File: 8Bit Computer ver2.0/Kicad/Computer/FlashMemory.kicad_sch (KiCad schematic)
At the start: 30 parts, among them IC189 SN74AHC74DR, IC190 M29F800FT55N3E2, IC191 DS1100Z-20+, IC192 M29F800FT55N3E2, IC193 SN74ABT245BDWR, IC194 SN74ABT245BDWR, IC195 SN74ABT245BDWR, IC196 SN74ABT245BDWR, IC197 SN74ABT245BDWR, IC198 SN74ABT245BDWR, IC199 SN74ABT245BDWR, IC200 SN74ABT245BDWR, IC201 SN74ABT245BDWR, IC202 SN74ABT245BDWR, IC203 SN74ABT245BDWR, IC204 SN74ABT245BDWR, IC205 SN74ABT245BDWR, IC206 SN74ABT245BDWR, J1 Conn_02x25_Odd_Even, J2 Conn_02x25_Odd_Even

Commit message: Kicad SCH/PCB
Kicad SCH/PCB:
changed the References in SCH
began with INOUTPUT module nearly done
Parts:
- renumbered IC191 to IC198, IC189 to IC199, IC194 to IC200, IC193 to IC201, IC197 to IC202, IC200 to IC203, IC201 to IC204, IC192 to IC205, IC202 to IC206, IC190 to IC207, IC195 to IC208, IC196 to IC209, IC203 to IC210, IC204 to IC211, IC198 to IC212, IC199 to IC213, IC205 to IC214, IC206 to IC215, J1 to J35, J2 to J36, R2 to R21, R1 to R22, R4 to R23, R6 to R24, R7 to R25, R8 to R26, R3 to R27, R5 to R28, R9 to R29, R10 to R30
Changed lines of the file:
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@@
 		(dnp no)
 		(fields_autoplaced yes)
-		(property "Reference" "IC191"
+		(property "Reference" "IC198"
 			(at 163.83 255.27 0)
 			(effects
@@
 			(project ""
 				(path "/1196a00e-6878-4d6d-82b7-9e052dfe7c14/51d10ac8-27e7-4c9f-83ea-98776ebc8169"
-					(reference "IC191")
+					(reference "IC198")
 					(unit 1)
 				)
@@
 		(dnp no)
 		(fields_autoplaced yes)
-		(property "Reference" "R5"
+		(property "Reference" "R28"
 			(at 449.58 397.5099 0)
 			(effects
@@
 			(project "Computer"
 				(path "/1196a00e-6878-4d6d-82b7-9e052dfe7c14/51d10ac8-27e7-4c9f-83ea-98776ebc8169"
-					(reference "R5")
+					(reference "R28")
 					(unit 1)
 				)
@@
 		(dnp no)
 		(fields_autoplaced yes)
-		(property "Reference" "IC204"
+		(property "Reference" "IC211"
 			(at 505.46 236.22 0)
 			(effects
@@
 			(project "Computer"
 				(path "/1196a00e-6878-4d6d-82b7-9e052dfe7c14/51d10ac8-27e7-4c9f-83ea-98776ebc8169"
-					(reference "IC204")
+					(reference "IC211")
 					(unit 1)
 				)
@@
 		(dnp no)
 		(fields_autoplaced yes)
-		(property "Reference" "J1"
+		(property "Reference" "J35"
 			(at 262.89 105.4099 90)
 			(effects
@@
 			(project ""
 				(path "/1196a00e-6878-4d6d-82b7-9e052dfe7c14/51d10ac8-27e7-4c9f-83ea-98776ebc8169"
-					(reference "J1")
+					(reference "J35")
 					(unit 1)
 				)
@@
 		(dnp no)
 		(fields_autoplaced yes)
-		(property "Reference" "IC205"
+		(property "Reference" "IC214"
 			(at 567.69 203.2 0)
 			(effects
@@
 			(project "Computer"
 				(path "/1196a00e-6878-4d6d-82b7-9e052dfe7c14/51d10ac8-27e7-4c9f-83ea-98776ebc8169"
-					(reference "IC205")
+					(reference "IC214")
 					(unit 1)
 				)
@@
 		(dnp no)
 		(fields_autoplaced yes)
-		(property "Reference" "R2"
+		(property "Reference" "R21"
 			(at 252.73 342.8999 0)
 			(effects
@@
 			(project "Computer"
 				(path "/1196a00e-6878-4d6d-82b7-9e052dfe7c14/51d10ac8-27e7-4c9f-83ea-98776ebc8169"
-					(reference "R2")
+					(reference "R21")
 					(unit 1)
 				)
@@
 		(dnp no)
 		(fields_autoplaced yes)
-		(property "Reference" "IC189"
+		(property "Reference" "IC199"
 			(at 219.71 292.1 0)
 			(effects
@@
 			(project ""
 				(path "/1196a00e-6878-4d6d-82b7-9e052dfe7c14/51d10ac8-27e7-4c9f-83ea-98776ebc8169"
-					(reference "IC189")
+					(reference "IC199")
 					(unit 1)
 				)
@@
 		(dnp no)
 		(fields_autoplaced yes)
-		(property "Reference" "IC193"
+		(property "Reference" "IC201"
 			(at 224.79 342.9 0)
 			(effects
@@
 			(project ""
 				(path "/1196a00e-6878-4d6d-82b7-9e052dfe7c14/51d10ac8-27e7-4c9f-83ea-98776ebc8169"
-					(reference "IC193")
+					(reference "IC201")
 					(unit 1)
 				)
@@
 		(dnp no)
 		(fields_autoplaced yes)
-		(property "Reference" "IC194"
+		(property "Reference" "IC200"
 			(at 223.52 386.08 0)
 			(effects
@@
 			(project "Computer"
 				(path "/1196a00e-6878-4d6d-82b7-9e052dfe7c14/51d10ac8-27e7-4c9f-83ea-98776ebc8169"
-					(reference "IC194")
+					(reference "IC200")
 					(unit 1)
 				)
@@
 		(dnp no)
 		(fields_autoplaced yes)
-		(property "Reference" "IC198"
+		(property "Reference" "IC212"
 			(at 513.08 350.52 0)
 			(effects
@@
 			(project "Computer"
 				(path "/1196a00e-6878-4d6d-82b7-9e052dfe7c14/51d10ac8-27e7-4c9f-83ea-98776ebc8169"
-					(reference "IC198")
+					(reference "IC212")
 					(unit 1)
 				)
@@
 		(dnp no)
 		(fields_autoplaced yes)
-		(property "Reference" "R7"
+		(property "Reference" "R25"
 			(at 287.02 227.3299 0)
 			(effects
@@
 			(project "Computer"
 				(path "/1196a00e-6878-4d6d-82b7-9e052dfe7c14/51d10ac8-27e7-4c9f-83ea-98776ebc8169"
-					(reference "R7")
+					(reference "R25")
 					(unit 1)
 				)
@@
 		(dnp no)
 		(fields_autoplaced yes)
-		(property "Reference" "IC196"
+		(property "Reference" "IC209"
 			(at 426.72 397.51 0)
 			(effects
@@
 			(project "Computer"
 				(path "/1196a00e-6878-4d6d-82b7-9e052dfe7c14/51d10ac8-27e7-4c9f-83ea-98776ebc8169"
-					(reference "IC196")
+					(reference "IC209")
 					(unit 1)
 				)
@@
 		(dnp no)
 		(fields_autoplaced yes)
-		(property "Reference" "IC202"
+		(property "Reference" "IC206"
 			(at 355.6 288.29 0)
 			(effects
@@
 			(project "Computer"
 				(path "/1196a00e-6878-4d6d-82b7-9e052dfe7c14/51d10ac8-27e7-4c9f-83ea-98776ebc8169"
-					(reference "IC202")
+					(reference "IC206")
 					(unit 1)
 				)
@@
 		(dnp no)
 		(fields_autoplaced yes)
-		(property "Reference" "R4"
+		(property "Reference" "R23"
 			(at 261.62 443.2299 0)
 			(effects
@@
 			(project "Computer"
 				(path "/1196a00e-6878-4d6d-82b7-9e052dfe7c14/51d10ac8-27e7-4c9f-83ea-98776ebc8169"
-					(reference "R4")
+					(reference "R23")
 					(unit 1)
 				)
@@
 		(dnp no)
 		(fields_autoplaced yes)
-		(property "Reference" "IC192"
+		(property "Reference" "IC205"
 			(at 303.53 347.98 0)
 			(effects
@@
 			(project "Computer"
 				(path "/1196a00e-6878-4d6d-82b7-9e052dfe7c14/51d10ac8-27e7-4c9f-83ea-98776ebc8169"
-					(reference "IC192")
+					(reference "IC205")
 					(unit 1)
 				)
@@
 		(dnp no)
 		(fields_autoplaced yes)
-		(property "Reference" "IC199"
+		(property "Reference" "IC213"
 			(at 513.08 394.97 0)
 			(effects
@@
 			(project "Computer"
 				(path "/1196a00e-6878-4d6d-82b7-9e052dfe7c14/51d10ac8-27e7-4c9f-83ea-98776ebc8169"
-					(reference "IC199")
+					(reference "IC213")
 					(unit 1)
 				)
@@
 		(dnp no)
 		(fields_autoplaced yes)
-		(property "Reference" "J2"
+		(property "Reference" "J36"
 			(at 438.15 105.4099 90)
 			(effects
@@
 			(project "Computer"
 				(path "/1196a00e-6878-4d6d-82b7-9e052dfe7c14/51d10ac8-27e7-4c9f-83ea-98776ebc8169"
-					(reference "J2")
+					(reference "J36")
 					(unit 1)
 				)
@@
 		(dnp no)
 		(fields_autoplaced yes)
-		(property "Reference" "IC206"
+		(property "Reference" "IC215"
 			(at 567.69 238.76 0)
 			(effects
@@
 			(project "Computer"
 				(path "/1196a00e-6878-4d6d-82b7-9e052dfe7c14/51d10ac8-27e7-4c9f-83ea-98776ebc8169"
-					(reference "IC206")
+					(reference "IC215")
 					(unit 1)
 				)
@@
 		(dnp no)
 		(fields_autoplaced yes)
-		(property "Reference" "IC197"
+		(property "Reference" "IC202"
 			(at 233.68 443.23 0)
 			(effects
@@
 			(project "Computer"
 				(path "/1196a00e-6878-4d6d-82b7-9e052dfe7c14/51d10ac8-27e7-4c9f-83ea-98776ebc8169"
-					(reference "IC197")
+					(reference "IC202")
 					(unit 1)
 				)
@@
 		(dnp no)
 		(fields_autoplaced yes)
-		(property "Reference" "IC190"
+		(property "Reference" "IC207"
 			(at 387.35 196.85 0)
 			(effects
@@
 			(project ""
 				(path "/1196a00e-6878-4d6d-82b7-9e052dfe7c14/51d10ac8-27e7-4c9f-83ea-98776ebc8169"
-					(reference "IC190")
+					(reference "IC207")
 					(unit 1)
 				)
@@
 		(dnp no)
 		(fields_autoplaced yes)
-		(property "Reference" "R6"
+		(property "Reference" "R24"
 			(at 287.02 184.1499 0)
 			(effects
@@
 			(project "Computer"
 				(path "/1196a00e-6878-4d6d-82b7-9e052dfe7c14/51d10ac8-27e7-4c9f-83ea-98776ebc8169"
-					(reference "R6")
+					(reference "R24")
 					(unit 1)
 				)
@@
 		(dnp no)
 		(fields_autoplaced yes)
-		(property "Reference" "IC200"
+		(property "Reference" "IC203"
 			(at 259.08 184.15 0)
 			(effects
@@
 			(project "Computer"
 				(path "/1196a00e-6878-4d6d-82b7-9e052dfe7c14/51d10ac8-27e7-4c9f-83ea-98776ebc8169"
-					(reference "IC200")
+					(reference "IC203")
 					(unit 1)
 				)
@@
 		(dnp no)
 		(fields_autoplaced yes)
-		(property "Reference" "IC201"
+		(property "Reference" "IC204"
 			(at 259.08 227.33 0)
 			(effects
@@
 			(project "Computer"
 				(path "/1196a00e-6878-4d6d-82b7-9e052dfe7c14/51d10ac8-27e7-4c9f-83ea-98776ebc8169"
-					(reference "IC201")
+					(reference "IC204")
 					(unit 1)
 				)
@@
 		(dnp no)
 		(fields_autoplaced yes)
-		(property "Reference" "R10"
+		(property "Reference" "R30"
 			(at 528.32 240.0299 0)
 			(effects
@@
 			(project "Computer"
 				(path "/1196a00e-6878-4d6d-82b7-9e052dfe7c14/51d10ac8-27e7-4c9f-83ea-98776ebc8169"
-					(reference "R10")
+					(reference "R30")
 					(unit 1)
 				)
@@
 		(dnp no)
 		(fields_autoplaced yes)
-		(property "Reference" "R3"
+		(property "Reference" "R27"
 			(at 414.02 353.0599 0)
 			(effects
@@
 			(project "Computer"
 				(path "/1196a00e-6878-4d6d-82b7-9e052dfe7c14/51d10ac8-27e7-4c9f-83ea-98776ebc8169"
-					(reference "R3")
+					(reference "R27")
 					(unit 1)
 				)
@@
 		(dnp no)
 		(fields_autoplaced yes)
-		(property "Reference" "R1"
+		(property "Reference" "R22"
 			(at 254 386.0799 0)
 			(effects
@@
 			(project ""
 				(path "/1196a00e-6878-4d6d-82b7-9e052dfe7c14/51d10ac8-27e7-4c9f-83ea-98776ebc8169"
-					(reference "R1")
+					(reference "R22")
 					(unit 1)
 				)
@@
 		(dnp no)
 		(fields_autoplaced yes)
-		(property "Reference" "IC195"
+		(property "Reference" "IC208"
 			(at 391.16 353.06 0)
 			(effects
@@
 			(project "Computer"
 				(path "/1196a00e-6878-4d6d-82b7-9e052dfe7c14/51d10ac8-27e7-4c9f-83ea-98776ebc8169"
-					(reference "IC195")
+					(reference "IC208")
 					(unit 1)
 				)
@@
 		(dnp no)
 		(fields_autoplaced yes)
-		(property "Reference" "R8"
+		(property "Reference" "R26"
 			(at 383.54 288.2899 0)
 			(effects
@@
 			(project "Computer"
 				(path "/1196a00e-6878-4d6d-82b7-9e052dfe7c14/51d10ac8-27e7-4c9f-83ea-98776ebc8169"
-					(reference "R8")
+					(reference "R26")
 					(unit 1)
 				)
@@
 		(dnp no)
 		(fields_autoplaced yes)
-		(property "Reference" "R9"
+		(property "Reference" "R29"
 			(at 528.32 200.6599 0)
 			(effects
@@
 			(project "Computer"
 				(path "/1196a00e-6878-4d6d-82b7-9e052dfe7c14/51d10ac8-27e7-4c9f-83ea-98776ebc8169"
-					(reference "R9")
+					(reference "R29")
 					(unit 1)
 				)
@@
 		(dnp no)
 		(fields_autoplaced yes)
-		(property "Reference" "IC203"
+		(property "Reference" "IC210"
 			(at 505.46 200.66 0)
 			(effects
@@
 			(project "Computer"
 				(path "/1196a00e-6878-4d6d-82b7-9e052dfe7c14/51d10ac8-27e7-4c9f-83ea-98776ebc8169"
-					(reference "IC203")
+					(reference "IC210")
 					(unit 1)
 				)

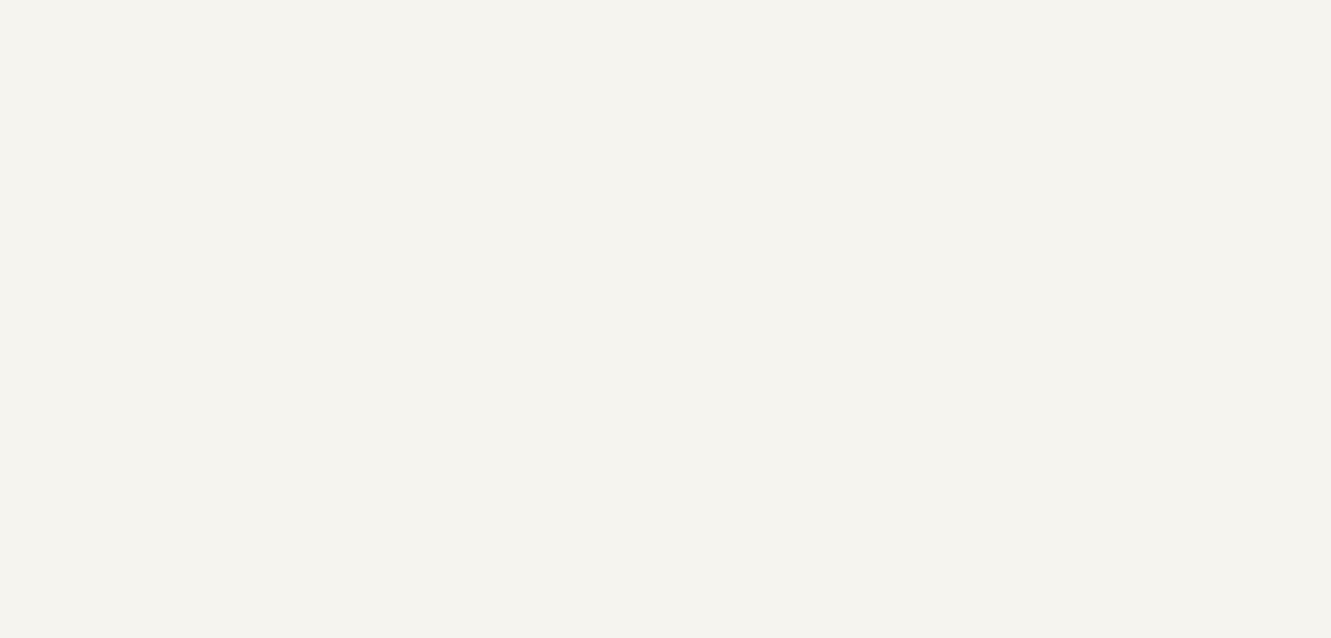
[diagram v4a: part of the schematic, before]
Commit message: Kicad,parts
parts:
added 1N4148 Diode SMD
Kicad:
fixed some routings of Schematic
created Flash mem and RAM PCB
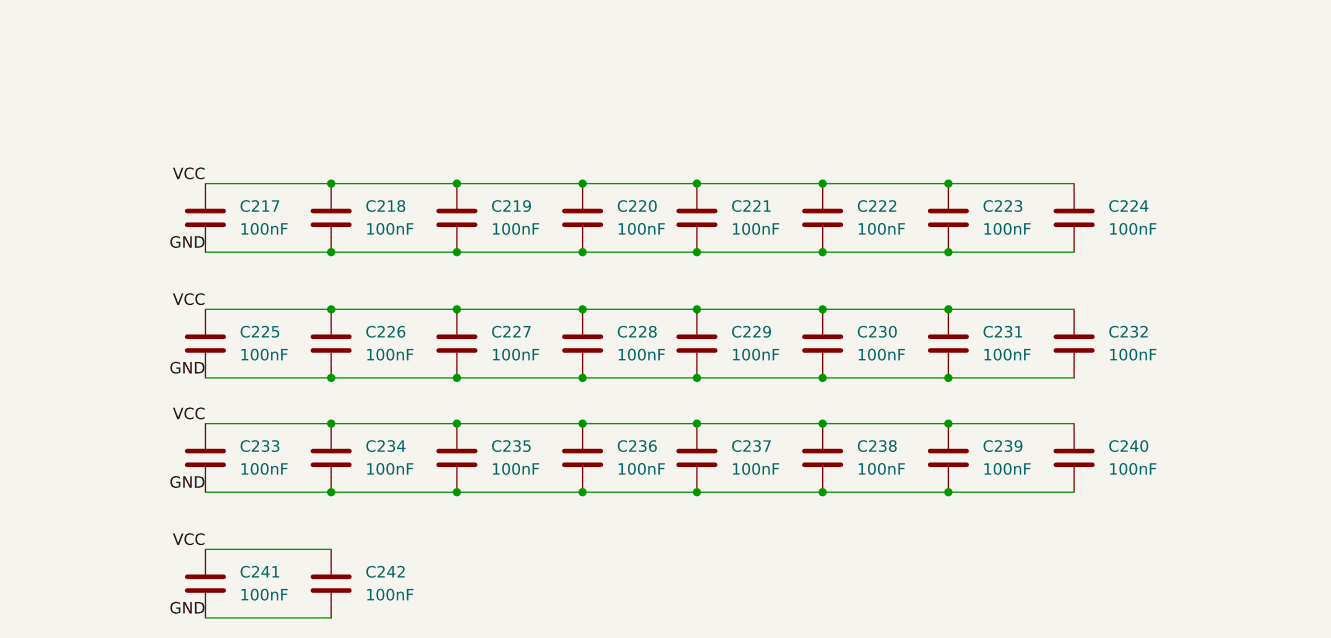
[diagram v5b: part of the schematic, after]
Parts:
- added C217, C218, C219, C220, C221, C222, C223, C224, C225, C226, C227, C228, C229, C230, C231, C232, C233, C234, C235, C236, C237, C238, C239, C240, C241, C242: 100nF, Capacitor_SMD:C_1206_3216Metric_Pad1.33x1.80mm_HandSolder, symbol Device:C
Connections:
- net GND: now also C217.1, C218.1, C219.1, C220.1, C221.1, C222.1, C223.1, C224.1, C225.1, C226.1, C227.1, C228.1, C229.1, C230.1, C231.1, C232.1, C233.1, C234.1, C235.1, C236.1, C237.1, C238.1, C239.1, C240.1, C241.1, C242.1
- net VCC: now also C217.2, C218.2, C219.2, C220.2, C221.2, C222.2, C223.2, C224.2, C225.2, C226.2, C227.2, C228.2, C229.2, C230.2, C231.2, C232.2, C233.2, C234.2, C235.2, C236.2, C237.2, C238.2, C239.2, C240.2, C241.2, C242.2
